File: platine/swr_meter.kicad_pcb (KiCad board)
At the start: 2 copper layers, 14 parts, among them U1 CP0x0xx5425xNTR_Directional_C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, U2 LTC5530, U3 LM1117_SOT223, U4 STM32F030C8Tx

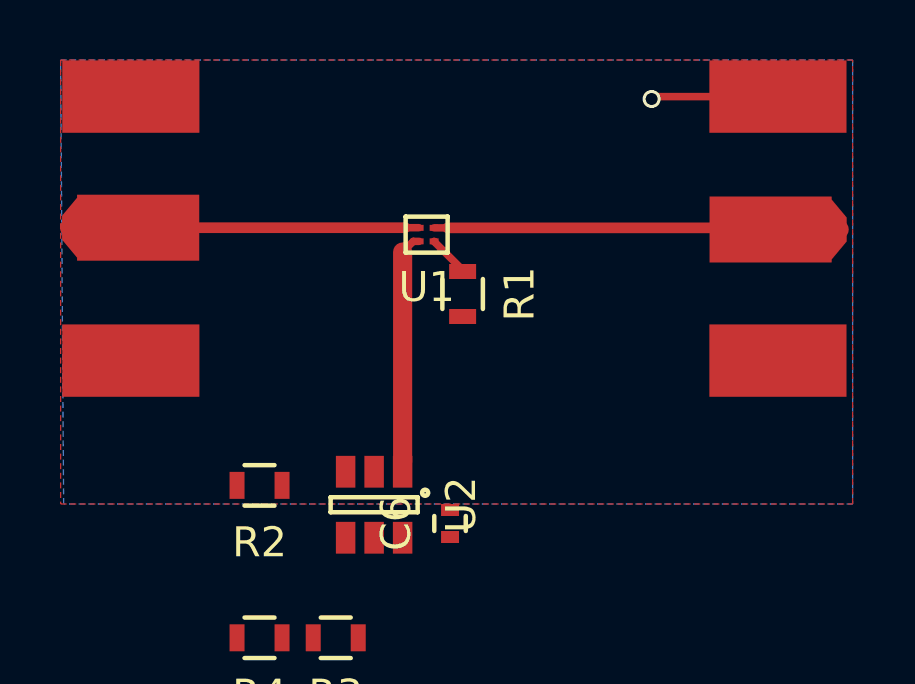
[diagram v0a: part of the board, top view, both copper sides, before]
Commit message: changed sma signal pads
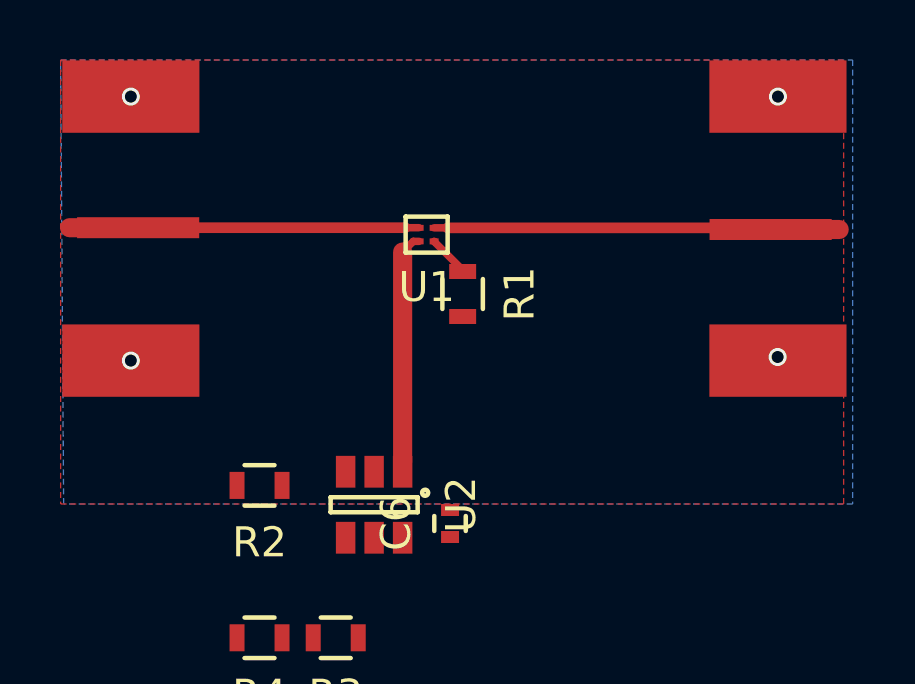
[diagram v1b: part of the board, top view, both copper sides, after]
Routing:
- net GND: track 4.38 -> 0.24 mm, vias 1 -> 4
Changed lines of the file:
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@@
   (general
     (links 27)
-    (no_connects 18)
+    (no_connects 17)
     (area 135.499499 90.644999 188.350501 130.575)
     (thickness 1.6)
     (drawings 0)
-    (tracks 18)
+    (tracks 26)
     (zones 0)
     (modules 14)
@@
     (mod_text_size 1 1)
     (mod_text_width 0.15)
-    (pad_size 1.524 1.524)
-    (pad_drill 0.762)
+    (pad_size 0.50038 0.4)
+    (pad_drill 0)
     (pad_to_mask_clearance 0.2)
     (aux_axis_origin 0 0)
@@
     (pad 0 connect rect (at -8.9 4.4 180) (size 4.572 2.413) (layers *.Mask F.Cu)
       (net 2 GND))
-    (pad 1 connect trapezoid (at -6.858 0.03 180) (size 0.50038 1.39954) (rect_delta 0.59944 0 ) (layers F.Cu F.Mask)
+    (pad 1 connect trapezoid (at -6.858 0.03 180) (size 0.50038 0.4) (rect_delta 0.2 0 ) (layers F.Cu F.Mask)
       (net 8 "Net-(SMA_E1-Pad1)"))
     (pad 2 connect rect (at -8.9 -4.4 180) (size 4.572 2.413) (layers *.Mask F.Cu)
       (net 2 GND))
-    (pad 1 connect rect (at -9.144 0.03 180) (size 4.07162 2.2) (layers F.Cu F.Mask)
+    (pad 1 connect rect (at -9.144 0.03 180) (size 4.07162 0.7) (layers F.Cu F.Mask)
       (net 8 "Net-(SMA_E1-Pad1)"))
     (model SMA_EDGE.wrl
@@
     (pad 0 connect rect (at -8.9 4.4) (size 4.572 2.413) (layers *.Mask F.Cu)
       (net 2 GND))
-    (pad 1 connect trapezoid (at -6.858 0.03) (size 0.50038 1.39954) (rect_delta 0.59944 0 ) (layers F.Cu F.Mask)
+    (pad 1 connect trapezoid (at -6.858 0.03) (size 0.50038 0.4) (rect_delta 0.2 0 ) (layers F.Cu F.Mask)
       (net 9 "Net-(SMA_E2-Pad1)"))
     (pad 2 connect rect (at -8.9 -4.4) (size 4.572 2.413) (layers *.Mask F.Cu)
       (net 2 GND))
-    (pad 1 connect rect (at -9.144 0.03) (size 4.07162 2.2) (layers F.Cu F.Mask)
+    (pad 1 connect rect (at -9.144 0.03) (size 4.07162 0.7) (layers F.Cu F.Mask)
       (net 9 "Net-(SMA_E2-Pad1)"))
     (model SMA_EDGE.wrl
@@
       (net 8 "Net-(SMA_E1-Pad1)"))
   )
-  (segment (start 172.71 92.12) (end 168.58 92.12) (width 0.25) (layer F.Cu) (net 2) (status 400000))
-  (segment (start 168.5 92.2) (end 168.6 92.1) (width 0.25) (layer B.Cu) (net 2))
-  (via (at 168.5 92.2) (size 0.6) (drill 0.4) (layers F.Cu B.Cu) (net 2))
-  (segment (start 168.58 92.12) (end 168.5 92.2) (width 0.25) (layer F.Cu) (net 2))
+  (via (at 151.14 100.92) (size 0.6) (drill 0.4) (layers F.Cu B.Cu) (net 2) (status C00000))
+  (segment (start 151.1 100.9) (end 151.12 100.9) (width 0.25) (layer B.Cu) (net 2))
+  (segment (start 151.12 100.9) (end 151.14 100.92) (width 0.25) (layer B.Cu) (net 2) (status 800000))
+  (via (at 151.14 92.12) (size 0.6) (drill 0.4) (layers F.Cu B.Cu) (net 2) (status C00000))
+  (segment (start 151.1 92.1) (end 151.12 92.1) (width 0.25) (layer B.Cu) (net 2))
+  (segment (start 151.12 92.1) (end 151.14 92.12) (width 0.25) (layer B.Cu) (net 2) (status 800000))
+  (via (at 172.7 100.8) (size 0.6) (drill 0.4) (layers F.Cu B.Cu) (net 2) (status 800000))
+  (segment (start 172.7 100.8) (end 172.71 100.81) (width 0.25) (layer F.Cu) (net 2) (status C00000))
+  (segment (start 172.71 100.81) (end 172.71 100.92) (width 0.25) (layer F.Cu) (net 2) (status C00000))
+  (via (at 172.71 92.12) (size 0.6) (drill 0.4) (layers F.Cu B.Cu) (net 2) (status C00000))
+  (segment (start 172.7 92.1) (end 172.7 92.11) (width 0.25) (layer B.Cu) (net 2))
+  (segment (start 172.7 92.11) (end 172.71 92.12) (width 0.25) (layer B.Cu) (net 2) (status 800000))
   (segment (start 161.25 96.945) (end 161.25 96.95) (width 0.25) (layer F.Cu) (net 5))
   (segment (start 161.25 96.95) (end 162.2 97.9) (width 0.25) (layer F.Cu) (net 5))
@@
     (polygon
       (pts
-        (xy 148.8 90.9) (xy 148.8 105.7) (xy 175.2 105.7) (xy 175.2 90.9)
+        (xy 148.8 90.9) (xy 148.8 105.7) (xy 174.9 105.7) (xy 174.9 90.9)
       )
     )

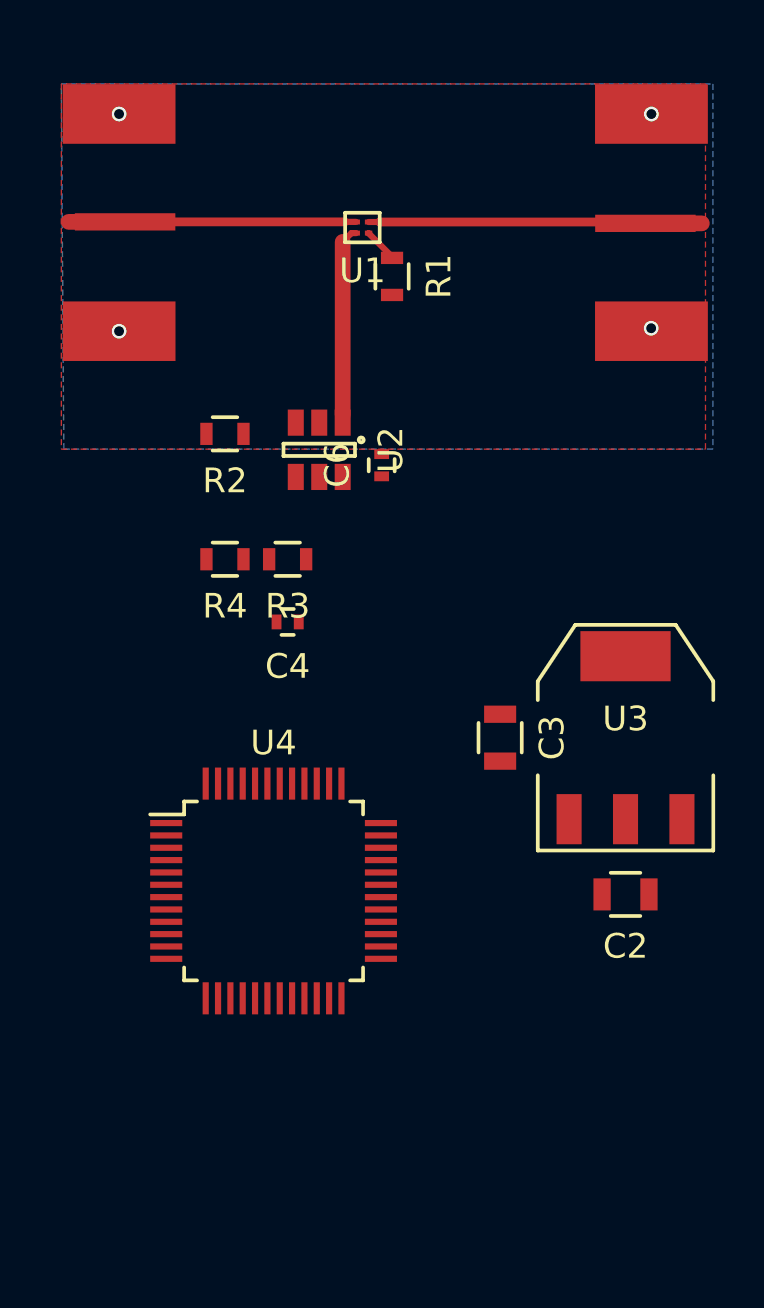
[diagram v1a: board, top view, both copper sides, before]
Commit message: HF Leiterbahnbreiten überarbeitet. HF-Teil fertig
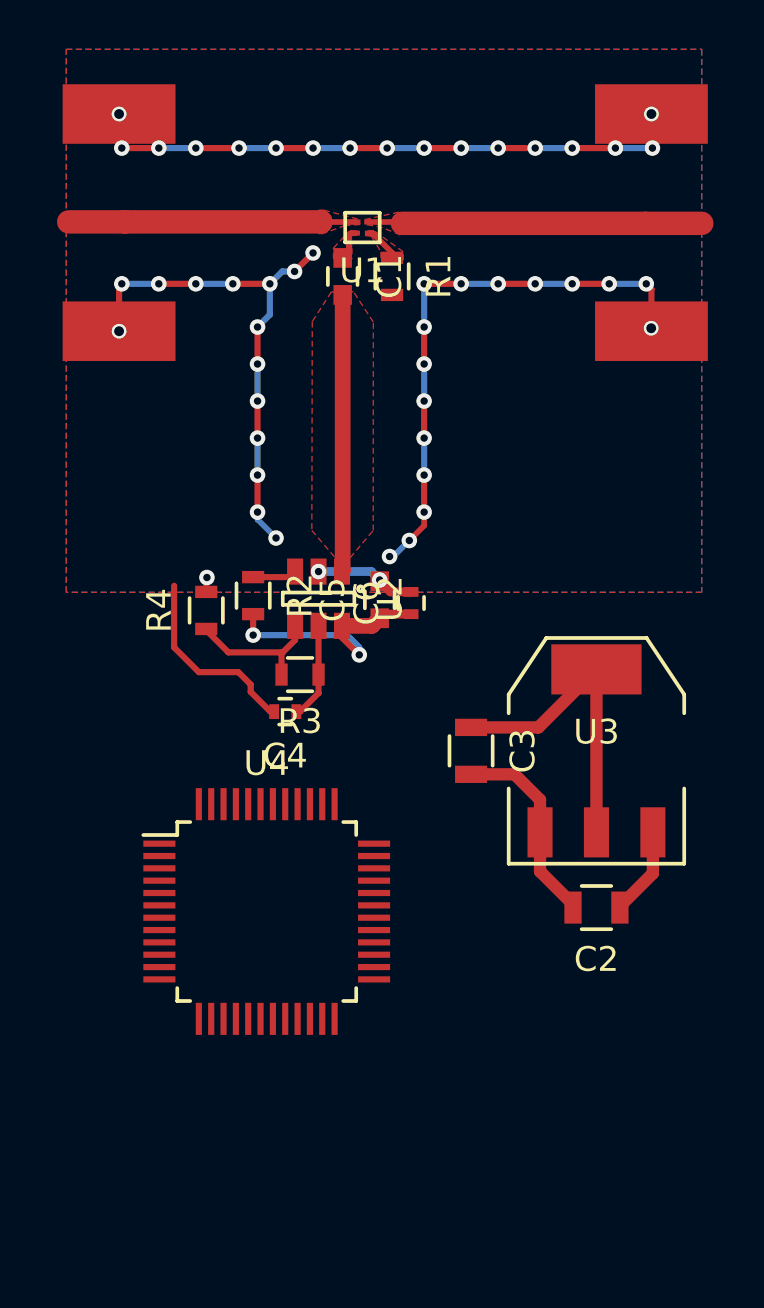
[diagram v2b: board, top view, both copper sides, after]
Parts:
- added C1: 39pF, Capacitors_SMD:C_0603, F.Cu at (160.2, 98.7)
- added C5: 100pF, Capacitors_SMD:C_0603, F.Cu at (161.7, 111.8)
- moved R2 6.65 mm to (156.6, 111.6), turned to 270 degrees
- moved U2 6.03 mm to (159.2, 111.8)
- moved C6 5.71 mm to (163.0, 111.9)
- moved R3 4.70 mm to (158.5, 114.8)
- moved C4 3.64 mm to (157.9, 116.3)
- moved R4 2.21 mm to (154.7, 112.2), turned to 90 degrees
- moved C3 1.29 mm to (165.4, 117.9)
- moved C2 1.29 mm to (170.5, 124.3)
- moved U3 1.29 mm to (170.5, 117.9)
- moved U4 0.88 mm to (157.1, 124.4)
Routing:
- net GND: track 0.24 -> 87.8 mm, vias 4 -> 51
- net +5V: track 0.00 -> 22.8 mm, vias 0 -> 2
- net Net-(R3-Pad2): track 0.00 -> 5.75 mm
- net Net-(C4-Pad1): track 0.00 -> 3.94 mm
- net Net-(C1-Pad2): track 7.60 -> 11.3 mm
- net Net-(C2-Pad1): track 0.00 -> 3.60 mm
- net Net-(R2-Pad1): track 0.00 -> 1.79 mm
- net Net-(C1-Pad1): track 0.19 -> 1.43 mm
- added copper zone on F.Cu, net Net-(C1-Pad1)
- added copper zone on F.Cu, net Net-(C1-Pad2)
- added copper zone on F.Cu, net Net-(R1-Pad1)
- added copper zone on F.Cu, net Net-(SMA_E1-Pad1)
- added copper zone on F.Cu, net Net-(SMA_E2-Pad1)
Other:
- net class Default: clearance 0.2 -> 0.15; via_dia 0.6 -> 0.63; via_drill 0.4 -> 0.3
- rule trace_clearance: 0.2 -> 0.15

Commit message: wiring of stm32
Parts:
- added C10: 100nF, Resistors_SMD:R_0402, F.Cu at (160.7, 130.2)
- added C7: 1uF, Capacitors_SMD:C_0603, F.Cu at (151.4, 125.3)
- added C8: 100nF, Resistors_SMD:R_0402, F.Cu at (151.8, 121.4)
- added C9: 100nF, Resistors_SMD:R_0402, F.Cu at (155.7, 118.0)
- added R5: 10R, Capacitors_SMD:C_0603, F.Cu at (149.7, 125.3)
- moved U4 1.06 mm to (158.1, 124.1)
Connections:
- net Net-(U4-Pad30) renamed /u1_tx
- net Net-(U4-Pad31) renamed /u1_rx
- net Net-(U4-Pad34) renamed /tms
- net Net-(U4-Pad37) renamed /tck
- net Net-(U4-Pad7) renamed /reset
- C3 pad 1: +5V -> +3V3
- C5 pad 1: +5V -> +3V3
- C6 pad 1: +5V -> +3V3
- R2 pad 2: +5V -> +3V3
- U2 pad 6: +5V -> +3V3
- U3 pad 2: +5V -> +3V3
- U3 pad 4: +5V -> +3V3
- U4 pad 1: Net-(U4-Pad1) -> +3V3
- U4 pad 11: Net-(U4-Pad11) -> Net-(C4-Pad1)
- U4 pad 23: Net-(U4-Pad23) -> GND
- U4 pad 24: Net-(U4-Pad24) -> +3V3
- U4 pad 44: Net-(U4-Pad44) -> GND
- U4 pad 47: Net-(U4-Pad47) -> GND
- U4 pad 48: Net-(U4-Pad48) -> +3V3
- U4 pad 8: Net-(U4-Pad8) -> GND
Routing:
- net +5V: track 22.8 -> 0.00 mm, vias 2 -> 0
- net +3V3: track 0.00 -> 22.8 mm, vias 0 -> 2

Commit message: routing of stm32
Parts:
- added U5: STM32_mmvisual_JTAG, Philipp:MICROMATCH-10, F.Cu at (171.4, 129.9)
- moved C3 3.98 mm to (165.9, 114.0)
- moved C2 3.98 mm to (170.9, 120.3)
- moved U3 3.98 mm to (170.9, 114.0)
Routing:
- net +3V3: track 22.8 -> 74.1 mm, vias 2 -> 4
- net GND: track 87.8 -> 119.9 mm, vias 51 -> 60
- net /reset: track 0.00 -> 19.9 mm
- net /u1_tx: track 0.00 -> 17.1 mm
- net /tck: track 0.00 -> 17.0 mm
- net /u1_rx: track 0.00 -> 15.9 mm
- net /tms: track 0.00 -> 11.6 mm
- net Net-(C7-Pad2): track 0.00 -> 4.37 mm

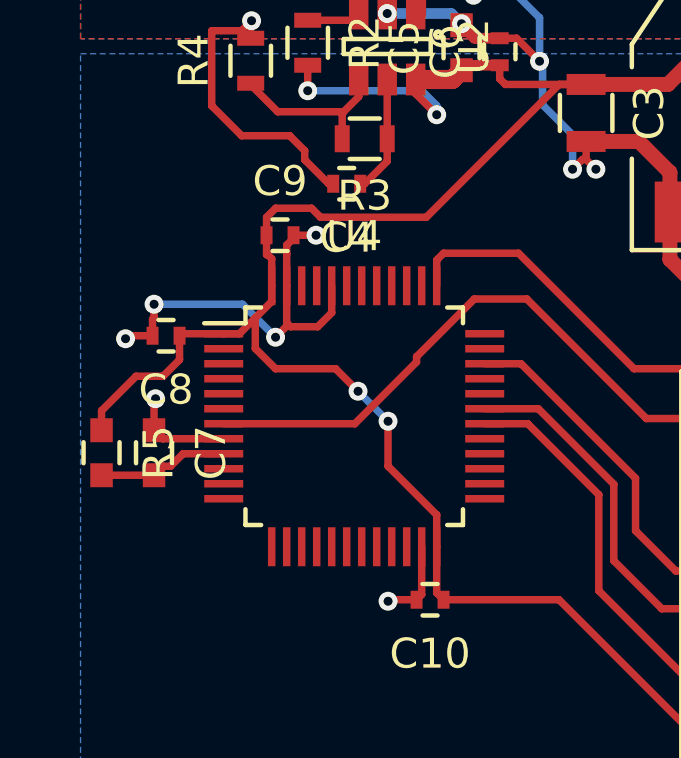
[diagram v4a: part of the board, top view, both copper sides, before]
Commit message: moved micromatch. finished except oled an seven-segment display
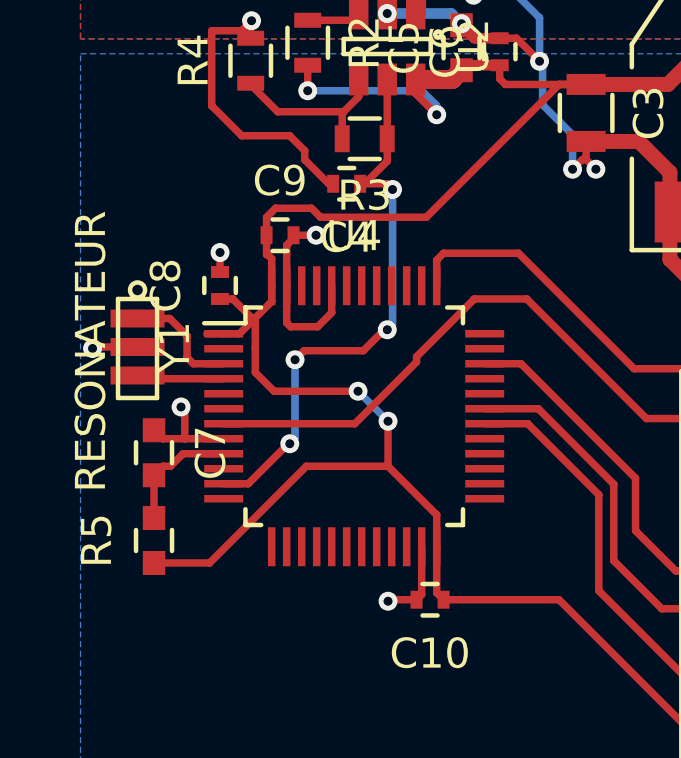
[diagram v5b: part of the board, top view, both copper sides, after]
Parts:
- added Y1: RESONATEUR, Toni:CerOsc_3,2x1,3, F.Cu at (150.9, 121.8)
- moved R5 3.41 mm to (151.4, 128.2), turned to 90 degrees
- moved C8 2.46 mm to (153.7, 119.7), turned to 90 degrees
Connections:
- net /tdi renamed Net-(U5-Pad6)
- net /tdo renamed Net-(U5-Pad2)
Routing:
- net Net-(C4-Pad1): track 3.94 -> 19.0 mm, vias 0 -> 4
- net +3V3: track 74.1 -> 79.5 mm
- net GND: track 119.9 -> 115.0 mm, vias 60 -> 59
- net Net-(U4-Pad3): track 0.00 -> 3.92 mm
- net Net-(U4-Pad4): track 0.00 -> 2.92 mm
